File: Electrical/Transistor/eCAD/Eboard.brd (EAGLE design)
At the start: 78.7 x 53.3 mm, 29 parts

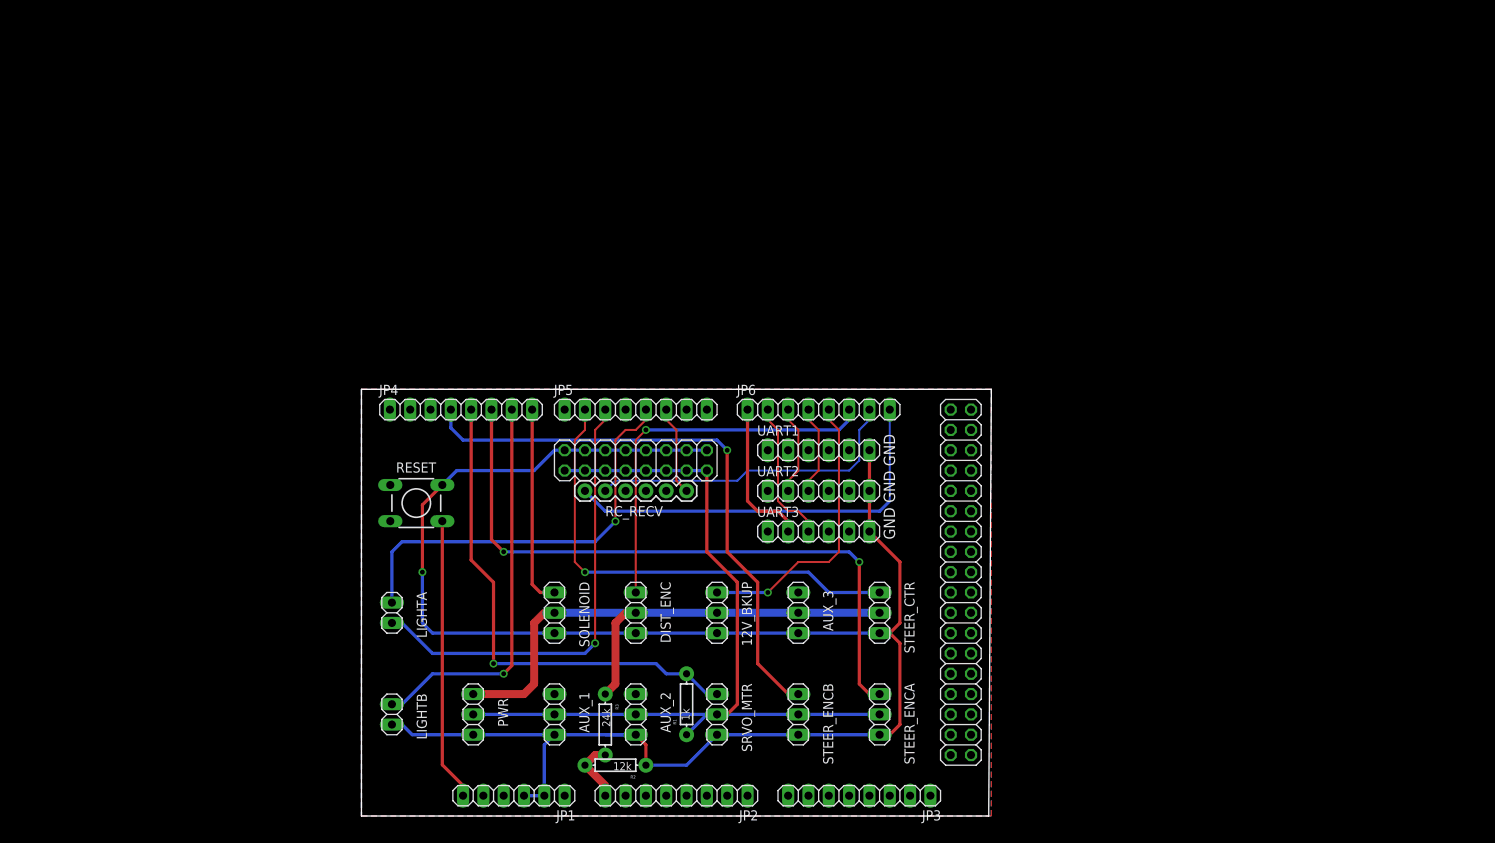
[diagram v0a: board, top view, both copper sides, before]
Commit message: shield updated with indicator lights, deleted excess pins, condensed encoder pins, deleted two aux pins, thickened 12V and 5V lines, connected 2 UARTs, 2 2-pin LEDs became 1 4-pin
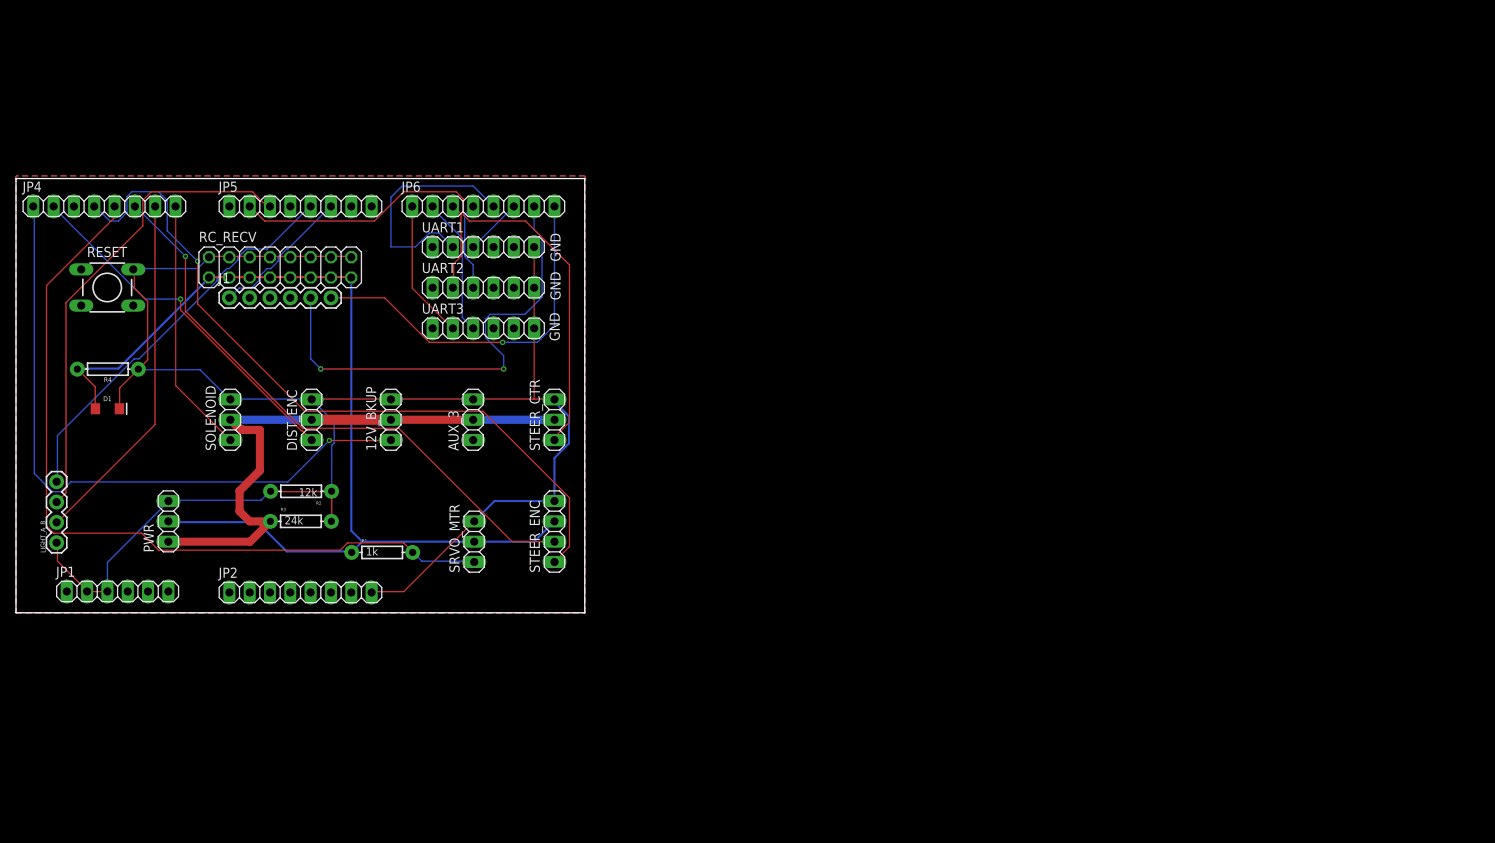
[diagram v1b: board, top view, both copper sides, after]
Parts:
- removed AUX_1, AUX_2, STEER_ENCA, STEER_ENCB: (no value), pinhead:1X03
- removed EXTRAS: (no value), pinhead:2X18
- removed JP3: (no value), pinhead:1X08
- removed LIGHTA, LIGHTB: (no value), pinhead:1X02
- added D1: (no value), SparkFun-LED:LED-1206
- added LIGHT_A_B: (no value), SparkFun-Connectors:1X04
- added R4: 1k, SparkFun-Resistors:AXIAL-0.3
- added STEER_ENC: (no value), pinhead:1X04
- moved J1 62.0 mm to (3.81, 64.8), turned to 0 degrees
- moved JP1 55.7 mm to (-10.2, 28.1), turned to 0 degrees
- moved JP2 53.4 mm to (12.7, 27.9), turned to 0 degrees
- moved R2 52.1 mm to (12.8, 40.6)
- moved JP4 51.3 mm to (-11.8, 76.2)
- moved RC_RECV 50.6 mm to (10.2, 68.6)
- moved JP5 49.0 mm to (12.7, 76.2)
- moved JP6 49.0 mm to (35.6, 76.2)
- moved UART1 49.0 mm to (35.6, 71.1)
- moved UART2 49.0 mm to (35.6, 66.0)
- moved UART3 49.0 mm to (35.6, 61.0)
- moved 12V_BKUP 47.4 mm to (24.0, 49.5), turned to 90 degrees
- moved AUX_3 47.3 mm to (34.3, 49.5), turned to 90 degrees
- moved STEER_CTR 47.3 mm to (44.5, 49.5), turned to 90 degrees
- moved DIST_ENC 47.2 mm to (14.1, 49.5), turned to 90 degrees
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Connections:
- net +12V renamed 12V
- net N$11 renamed UART3_TX
- net N$12 renamed UART3_RX
- net N$13 renamed UART2_TX
- net N$14 renamed UART2_RX
- net N$15 renamed J1_5
- net N$16 renamed J1_1
- net N$3 renamed J1_6
- net N$6 renamed SOLENOID
- net N$7 renamed STEER_CTR
- net N$8 renamed SRVO_MTR
- removed net N$1: JP2.8, R2.P$2, R3.P$2
- removed net N$10: JP4.6, STEER_ENCA.1
- removed net N$17: JP5.5, LIGHTA.1
- removed net N$18: JP5.3, LIGHTA.2
- removed net N$2: JP4.7, LIGHTB.1
- removed net N$9: JP4.4, STEER_ENCB.1
- removed net RESET: JP1.6, RESET.4
- new net 12V_BKUP: 12V_BKUP.1, JP4.1
- new net DIST_ENC: DIST_ENC.1, JP4.2
- new net LIGHT_A1: JP5.5, LIGHT_A_B.4
- new net LIGHT_A2: JP5.3, LIGHT_A_B.3
- new net LIGHT_B: JP4.7, LIGHT_A_B.2
- new net STEER_ENC1: JP4.4, STEER_ENC.1
- new net STEER_ENC2: JP4.6, STEER_ENC.2
- new net UART1_RX: JP6.6, UART1.3
- new net UART1_TX: JP6.5, UART1.2
- net 5V: now also D1.A, R4.P$2, STEER_ENC.3; no longer AUX_1.2, AUX_2.2, STEER_ENCA.2, STEER_ENCB.2
- net GND: now also D1.C, JP2.8, LIGHT_A_B.1, R2.P$2, R3.P$2, R4.P$1, STEER_ENC.4; no longer AUX_1.3, AUX_2.3, LIGHTB.2, STEER_ENCA.3, STEER_ENCB.3
- net N$4: now also JP1.6; no longer DIST_ENC.1, JP6.6
- net N$5: now also RESET.4; no longer 12V_BKUP.1, JP6.5
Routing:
- net STEER_ENC1: track 0.00 -> 92.8 mm, vias 0 -> 1
- net N$10: track 82.1 -> 0.00 mm, vias 2 -> 0
- net 12V_BKUP: track 0.00 -> 81.7 mm, vias 0 -> 1
- net STEER_ENC2: track 0.00 -> 73.8 mm, vias 0 -> 1
- net N$9: track 72.9 -> 0.00 mm, vias 1 -> 0
- net LIGHT_A2: track 0.00 -> 59.3 mm
- net N$18: track 57.2 -> 0.00 mm, vias 1 -> 0
- net N$17: track 52.2 -> 0.00 mm, vias 1 -> 0
- net LIGHT_A1: track 0.00 -> 49.7 mm
- net N$2: track 49.0 -> 0.00 mm, vias 1 -> 0
- net N$4: track 48.0 -> 0.00 mm, vias 1 -> 0
- net DIST_ENC: track 0.00 -> 45.4 mm, vias 0 -> 1
- net LIGHT_B: track 0.00 -> 44.7 mm
- net SRVO_MTR: track 62.4 -> 99.6 mm, vias 1 -> 0
- net N$5: track 35.7 -> 0.00 mm, vias 1 -> 0
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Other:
- board size 78.7 x 53.3 mm -> 71.1 x 54.3 mm
- board text added: "GND"
- board text added: "ROBOBUGGY REV 1.6"
- board text removed: "GND GND GND"
- board text removed: "Robobuggy rev 1.5"

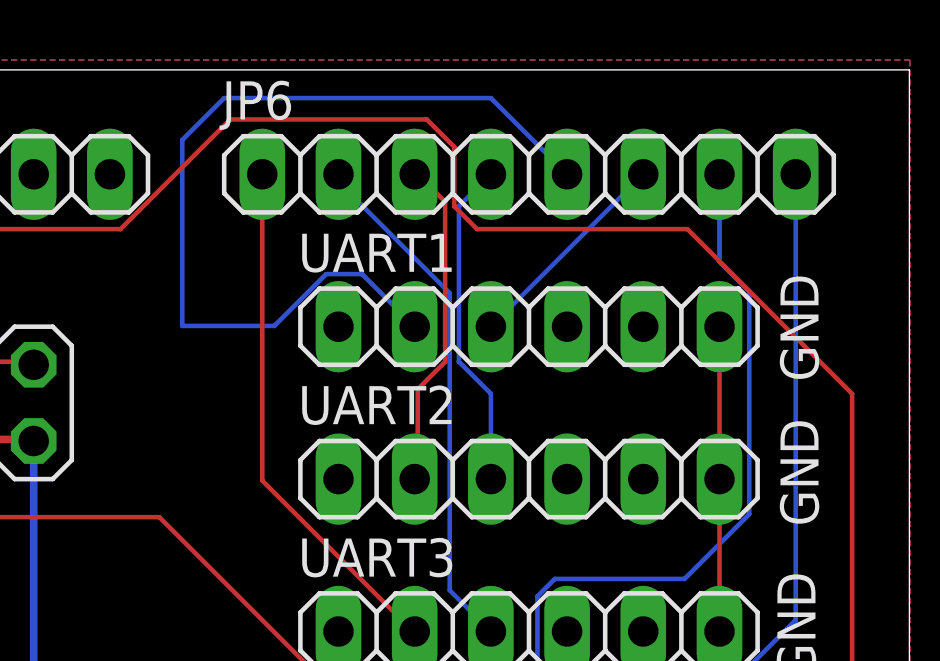
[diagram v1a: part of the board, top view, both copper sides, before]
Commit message: deleted UART1 because conflicts with the servo
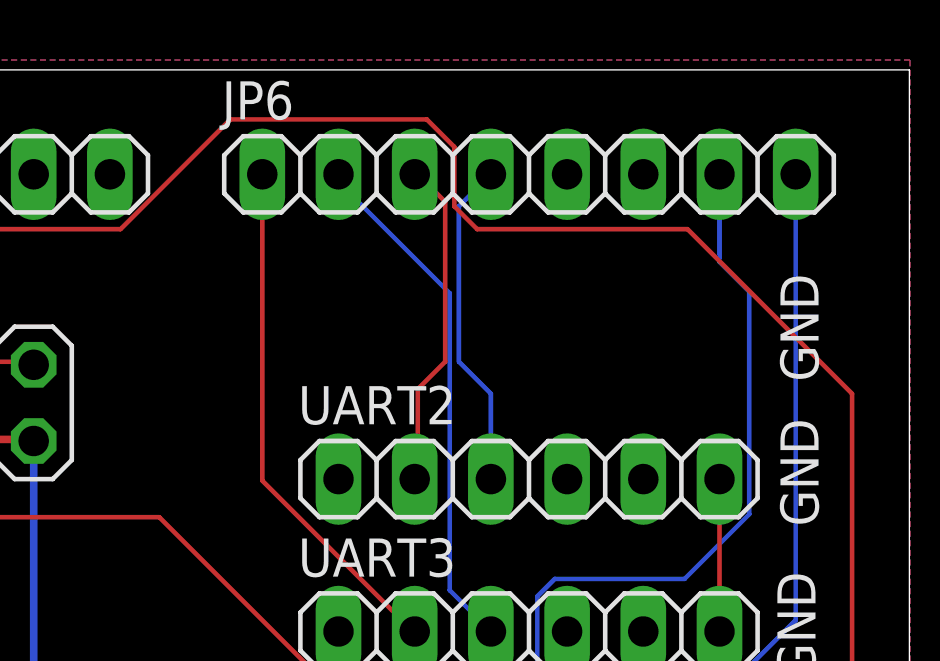
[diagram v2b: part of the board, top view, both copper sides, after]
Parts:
- removed UART1: (no value), pinhead:1X06
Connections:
- removed net UART1_RX: JP6.6, UART1.3
- removed net UART1_TX: JP6.5, UART1.2
- net GND: no longer UART1.6
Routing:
- net UART1_TX: track 29.8 -> 0.00 mm
- net UART1_RX: track 7.18 -> 0.00 mm
- net GND: track 225.1 -> 220.1 mm
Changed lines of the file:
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@@
 <element name="STEER_CTR" library="pinhead" package="1X03" value="" x="44.45" y="49.53" rot="R90"/>
 <element name="STEER_ENC" library="pinhead" library_urn="urn:adsk.eagle:library:325" package="1X04" package3d_urn="urn:adsk.eagle:package:22407/2" value="" x="44.45" y="35.56" rot="R90"/>
-<element name="UART1" library="pinhead" package="1X06" value="" x="35.56" y="71.12"/>
 <element name="UART2" library="pinhead" package="1X06" value="" x="35.56" y="66.04"/>
 <element name="UART3" library="pinhead" package="1X06" value="" x="35.56" y="60.96"/>
@@
 <contactref element="R4" pad="P$1"/>
 <contactref element="UART2" pad="6"/>
-<contactref element="UART1" pad="6"/>
 <contactref element="UART3" pad="6"/>
 <contactref element="R3" pad="P$2"/>
@@
 <wire x1="44.3484" y1="52.1208" x2="44.45" y2="52.07" width="0.1524" layer="1"/>
 <wire x1="41.91" y1="66.04" x2="41.91" y2="60.96" width="0.1524" layer="1"/>
-<wire x1="41.91" y1="66.04" x2="41.91" y2="71.12" width="0.1524" layer="1"/>
 <wire x1="41.91" y1="60.96" x2="41.91" y2="52.1208" width="0.1524" layer="1"/>
 <wire x1="8.8392" y1="69.9516" x2="6.4008" y2="69.9516" width="0.1524" layer="1"/>
@@
 <wire x1="34.29" y1="76.2" x2="33.2232" y2="75.1332" width="0.1524" layer="16"/>
 </signal>
-<signal name="UART1_TX">
-<contactref element="UART1" pad="2"/>
-<contactref element="JP6" pad="5"/>
-<wire x1="27.072475" y1="71.1454" x2="24.003" y2="71.1454" width="0.1524" layer="16"/>
-<wire x1="28.799675" y1="72.8726" x2="27.072475" y2="71.1454" width="0.1524" layer="16"/>
-<wire x1="31.75" y1="71.12" x2="29.9974" y2="72.8726" width="0.1524" layer="16"/>
-<wire x1="29.9974" y1="72.8726" x2="28.799675" y2="72.8726" width="0.1524" layer="16"/>
-<wire x1="24.003" y1="71.1454" x2="24.003" y2="77.343" width="0.1524" layer="16"/>
-<wire x1="24.003" y1="77.343" x2="25.4" y2="78.74" width="0.1524" layer="16"/>
-<wire x1="25.4" y1="78.74" x2="34.29" y2="78.74" width="0.1524" layer="16"/>
-<wire x1="34.29" y1="78.74" x2="36.83" y2="76.2" width="0.1524" layer="16"/>
-</signal>
-<signal name="UART1_RX">
-<contactref element="UART1" pad="3"/>
-<contactref element="JP6" pad="6"/>
-<wire x1="34.29" y1="71.12" x2="39.37" y2="76.2" width="0.1524" layer="16"/>
-</signal>
 <signal name="UART3_TX">

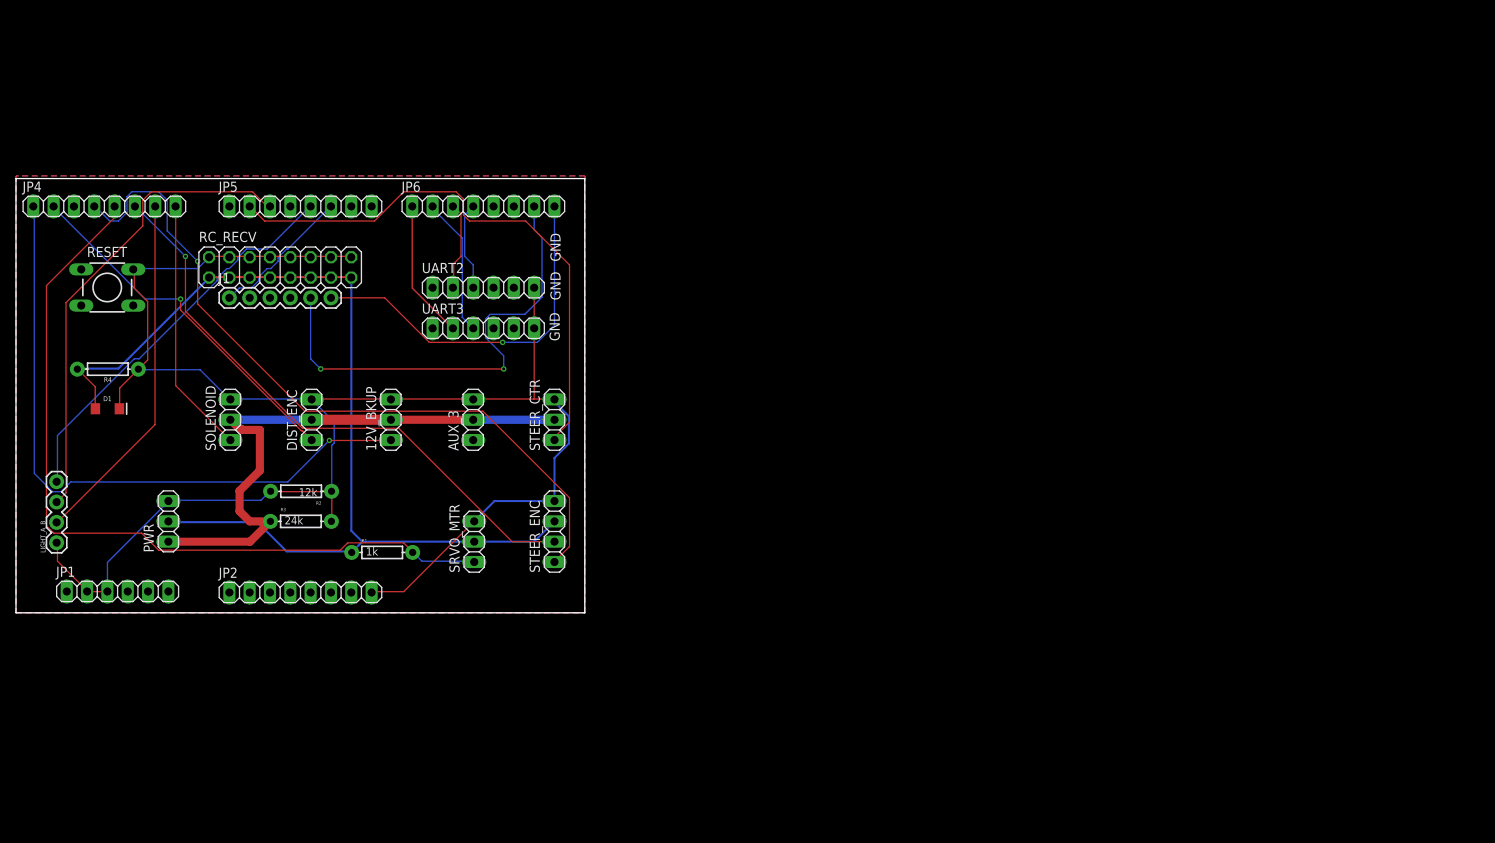
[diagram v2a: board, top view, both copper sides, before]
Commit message: deleted 12V_BKUP and AUX_3, as well as labelled everything. did not update .brd file yet.
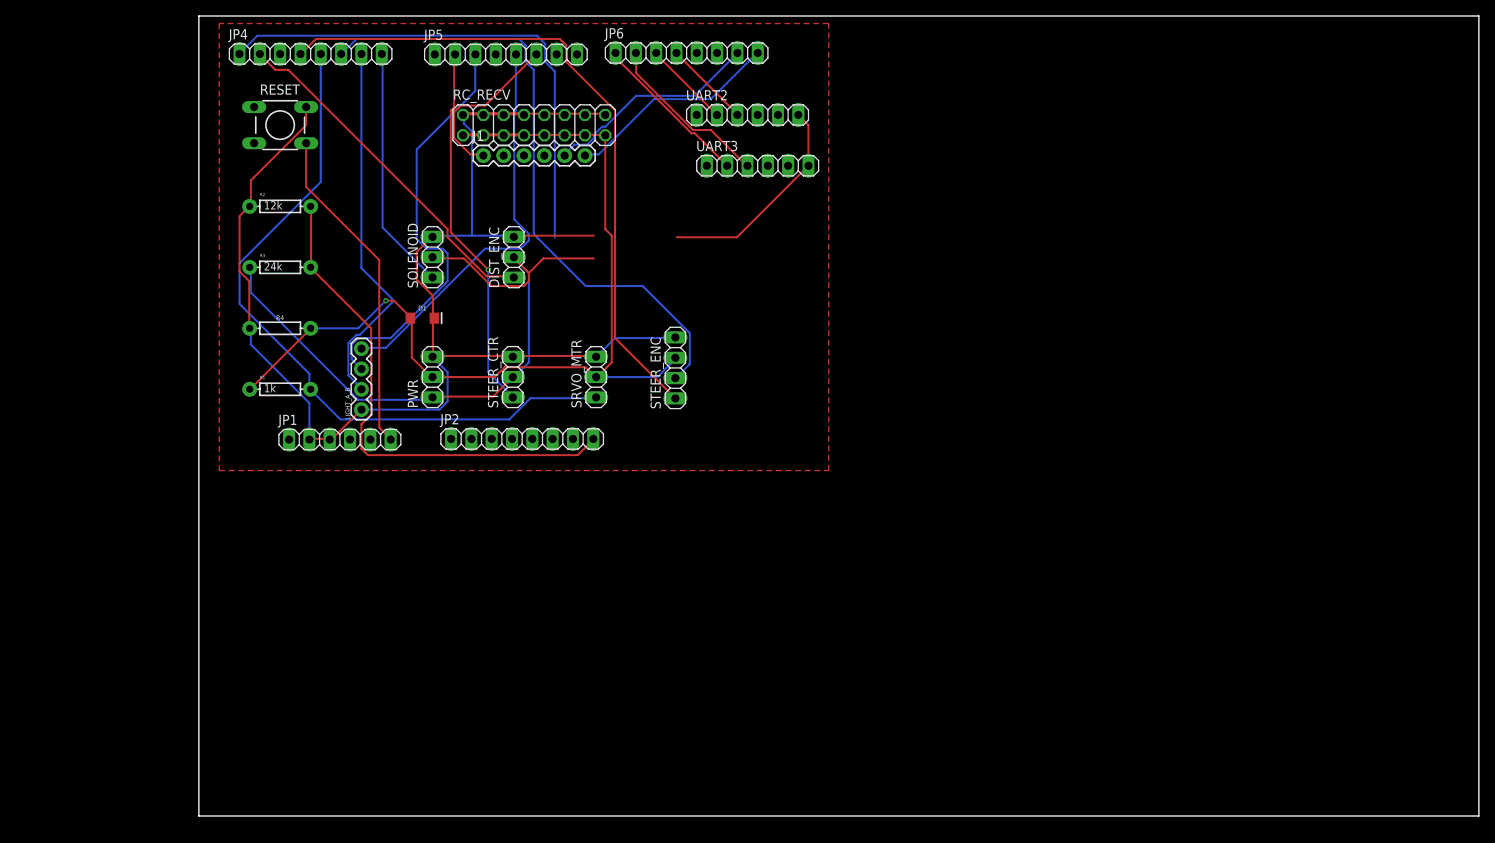
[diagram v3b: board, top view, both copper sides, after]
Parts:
- removed 12V_BKUP, AUX_3: (no value), pinhead:1X03
- moved LIGHT_A_B 41.6 mm to (20.3, 50.8)
- moved D1 41.0 mm to (27.9, 62.2)
- moved UART3 39.9 mm to (69.8, 81.3)
- moved UART2 39.5 mm to (68.6, 87.6)
- moved PWR 37.6 mm to (29.2, 54.9)
- moved J1 36.4 mm to (35.6, 82.5)
- moved RC_RECV 36.4 mm to (41.9, 86.4)
- moved R2 35.7 mm to (10.2, 76.2), turned to 0 degrees
- moved JP2 33.7 mm to (40.4, 47.1)
- moved JP1 33.7 mm to (17.6, 47.1)
- moved DIST_ENC 32.4 mm to (39.4, 69.8)
- moved SOLENOID 32.4 mm to (29.2, 69.8)
- moved JP4 32.1 mm to (14.0, 95.2)
- moved JP5 31.9 mm to (38.4, 95.2)
- moved R3 31.9 mm to (10.2, 68.6)
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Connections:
- removed net N$4: JP1.6
- removed net N$5: RESET.4
- removed net VCC: JP1.5
- new net SWITCH: JP1.6, RESET.4
- new net VBATT_ADC: JP2.8, R2.P$2, R3.P$2
- net 12V: no longer 12V_BKUP.2, AUX_3.2
- net 12V_BKUP: no longer 12V_BKUP.1
- net GND: no longer 12V_BKUP.3, AUX_3.3, JP2.8, R2.P$2, R3.P$2
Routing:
- net VBATT_ADC: track 0.00 -> 64.1 mm
- net SWITCH: track 0.00 -> 41.4 mm
- net J1_5: track 59.4 -> 27.2 mm, vias 2 -> 0
- net STEER_CTR: track 69.9 -> 46.3 mm, vias 0 -> 1
- net J1_6: track 46.0 -> 26.9 mm, vias 1 -> 0
- net 12V_BKUP: track 81.7 -> 64.3 mm, vias 1 -> 0
- net GND: track 220.1 -> 205.1 mm
- net 5V: track 130.4 -> 116.4 mm, vias 0 -> 1
- net SRVO_MTR: track 99.6 -> 88.2 mm
- net 12V: track 74.5 -> 85.9 mm
- net STEER_ENC1: track 92.8 -> 84.1 mm, vias 1 -> 0
- net LIGHT_A2: track 59.3 -> 53.0 mm
- net STEER_ENC2: track 73.8 -> 79.2 mm, vias 1 -> 0
- net UART3_RX: track 17.4 -> 21.2 mm
- net J1_1: track 18.0 -> 21.2 mm
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- added copper zone on layer 1, net N$1
- removed copper zone on layer 1, net GND
- removed copper zone on layer 16, net GND
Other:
- board size 71.1 x 54.3 mm -> 160 x 100 mm
- board text removed: "GND"
- board text removed: "ROBOBUGGY REV 1.6"
